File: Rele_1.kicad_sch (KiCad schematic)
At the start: 5 parts

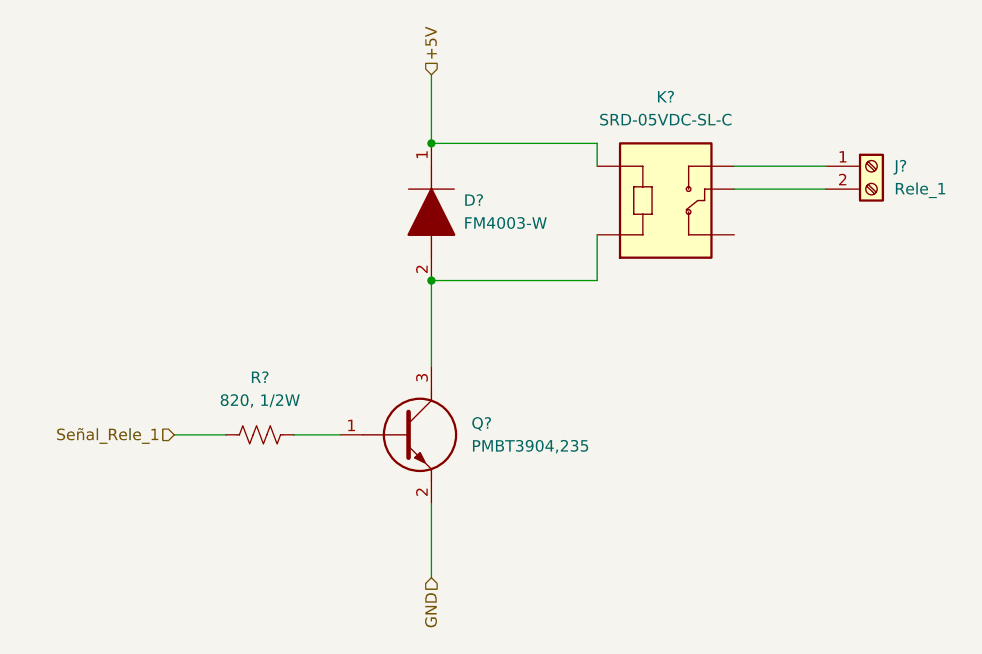
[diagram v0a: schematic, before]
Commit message: Ajuste del esquematico
Se cambio el integrado ESP32 por 2 tiras de pines de 1x15, se quitaron los switches EN y BOOT que ya estan en el NodeMCU, se quito el mutliplexor 74HC y se cablearon las I/O
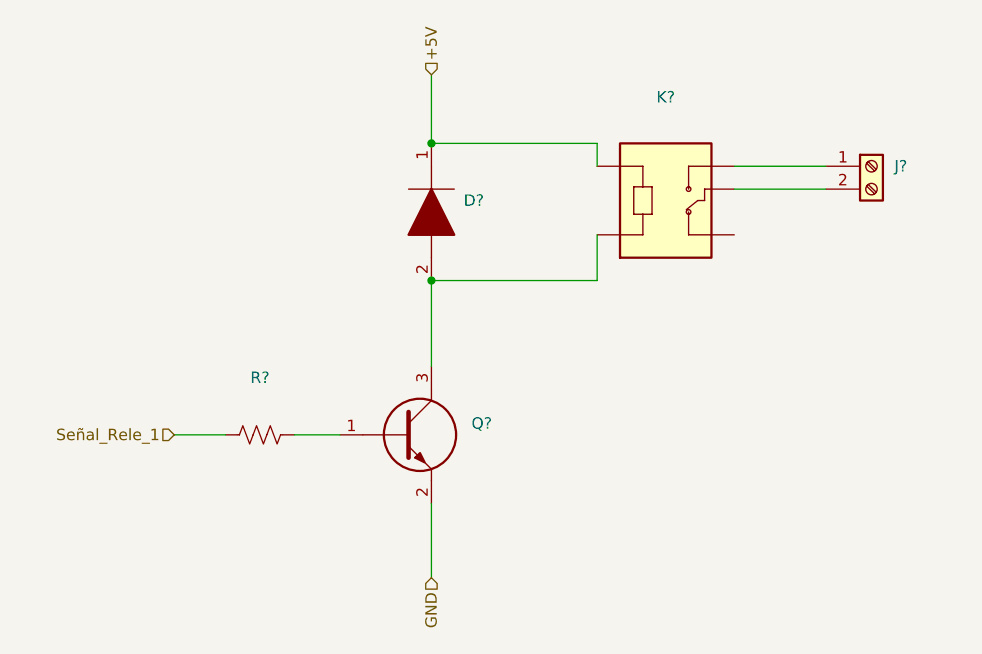
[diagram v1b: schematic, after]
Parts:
- D?: value FM4003-W -> (none); footprint DIOM5025X231N -> (none)
- J?: value Rele_1 -> (none)
- K?: value SRD-05VDC-SL-C -> (none); footprint RELAY_SRD-05VDC-SL-C -> (none)
- Q?: value PMBT3904,235 -> (none); footprint SOT95P230X110-3N -> (none)
- R?: value 820, 1/2W -> (none)
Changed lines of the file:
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@@
       (effects (font (size 1.27 1.27)) (justify left))
     )
-    (property "Value" "FM4003-W" (id 1) (at 143.2814 78.7399 90)
+    (property "Value" "" (id 1) (at 143.2814 78.7399 90)
       (effects (font (size 1.27 1.27)) (justify left))
     )
-    (property "Footprint" "DIOM5025X231N" (id 2) (at 139.7 81.28 0)
+    (property "Footprint" "" (id 2) (at 139.7 81.28 0)
       (effects (font (size 1.27 1.27)) (justify left) hide)
     )
@@
     (in_bom yes) (on_board yes) (fields_autoplaced)
     (property "Reference" "K?" (id 0) (at 165.735 64.7192 0))
-    (property "Value" "SRD-05VDC-SL-C" (id 1) (at 165.735 67.2592 0))
-    (property "Footprint" "RELAY_SRD-05VDC-SL-C" (id 2) (at 165.735 74.93 0)
+    (property "Value" "" (id 1) (at 165.735 67.2592 0))
+    (property "Footprint" "" (id 2) (at 165.735 74.93 0)
       (effects (font (size 1.27 1.27)) (justify left bottom) hide)
     )
@@
       (effects (font (size 1.27 1.27)) (justify left))
     )
-    (property "Value" "Rele_1" (id 1) (at 191.135 74.9299 0)
+    (property "Value" "" (id 1) (at 191.135 74.9299 0)
       (effects (font (size 1.27 1.27)) (justify left))
     )
@@
       (effects (font (size 1.27 1.27)) (justify left))
     )
-    (property "Value" "PMBT3904,235" (id 1) (at 144.145 103.5049 0)
+    (property "Value" "" (id 1) (at 144.145 103.5049 0)
       (effects (font (size 1.27 1.27)) (justify left))
     )
-    (property "Footprint" "SOT95P230X110-3N" (id 2) (at 143.51 106.045 0)
+    (property "Footprint" "" (id 2) (at 143.51 106.045 0)
       (effects (font (size 1.27 1.27)) (justify left) hide)
     )
@@
     (in_bom yes) (on_board yes) (fields_autoplaced)
     (property "Reference" "R?" (id 0) (at 120.65 95.885 90))
-    (property "Value" "820, 1/2W" (id 1) (at 120.65 98.425 90))
+    (property "Value" "" (id 1) (at 120.65 98.425 90))
     (property "Footprint" "" (id 2) (at 120.904 101.219 90)
       (effects (font (size 1.27 1.27)) hide)

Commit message: Modificación de posición de circ. filtrado y circ. de adaptación de tensión
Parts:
- D?, J?, K?, Q?, R?: value (none) -> ~
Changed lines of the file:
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@@
       (effects (font (size 1.27 1.27)) (justify left))
     )
-    (property "Value" "" (id 1) (at 143.2814 78.7399 90)
+    (property "Value" "~" (id 1) (at 143.2814 78.7399 90)
       (effects (font (size 1.27 1.27)) (justify left))
     )
@@
     (in_bom yes) (on_board yes) (fields_autoplaced)
     (property "Reference" "K?" (id 0) (at 165.735 64.7192 0))
-    (property "Value" "" (id 1) (at 165.735 67.2592 0))
+    (property "Value" "~" (id 1) (at 165.735 67.2592 0))
     (property "Footprint" "" (id 2) (at 165.735 74.93 0)
       (effects (font (size 1.27 1.27)) (justify left bottom) hide)
@@
       (effects (font (size 1.27 1.27)) (justify left))
     )
-    (property "Value" "" (id 1) (at 191.135 74.9299 0)
+    (property "Value" "~" (id 1) (at 191.135 74.9299 0)
       (effects (font (size 1.27 1.27)) (justify left))
     )
@@
       (effects (font (size 1.27 1.27)) (justify left))
     )
-    (property "Value" "" (id 1) (at 144.145 103.5049 0)
+    (property "Value" "~" (id 1) (at 144.145 103.5049 0)
       (effects (font (size 1.27 1.27)) (justify left))
     )
@@
     (in_bom yes) (on_board yes) (fields_autoplaced)
     (property "Reference" "R?" (id 0) (at 120.65 95.885 90))
-    (property "Value" "" (id 1) (at 120.65 98.425 90))
+    (property "Value" "~" (id 1) (at 120.65 98.425 90))
     (property "Footprint" "" (id 2) (at 120.904 101.219 90)
       (effects (font (size 1.27 1.27)) hide)

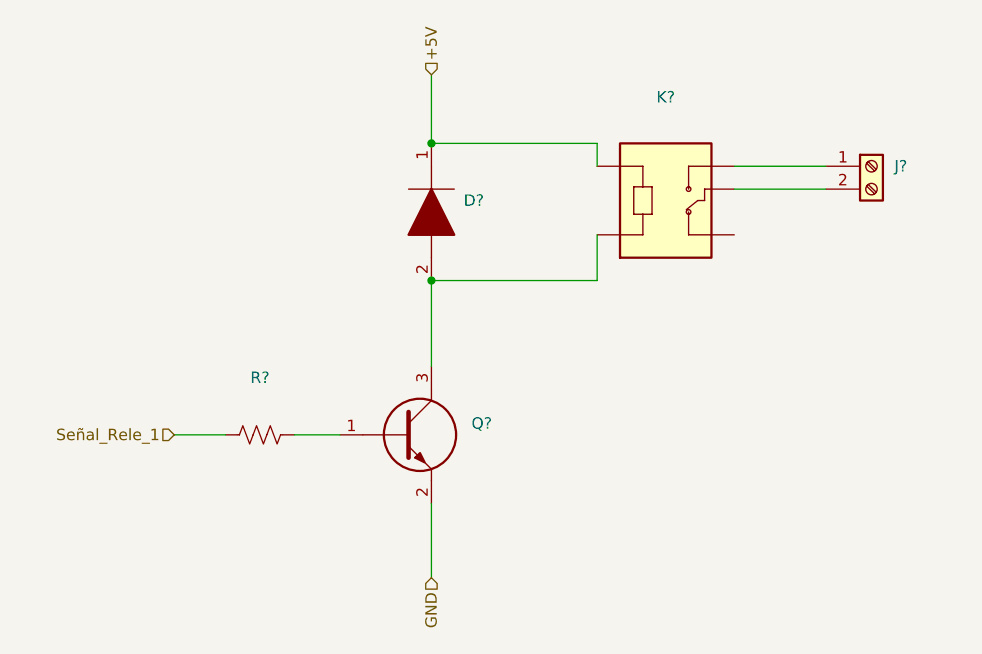
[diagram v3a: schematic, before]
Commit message: Actualización de SCH según placa industrial, y búsqueda de footprints.
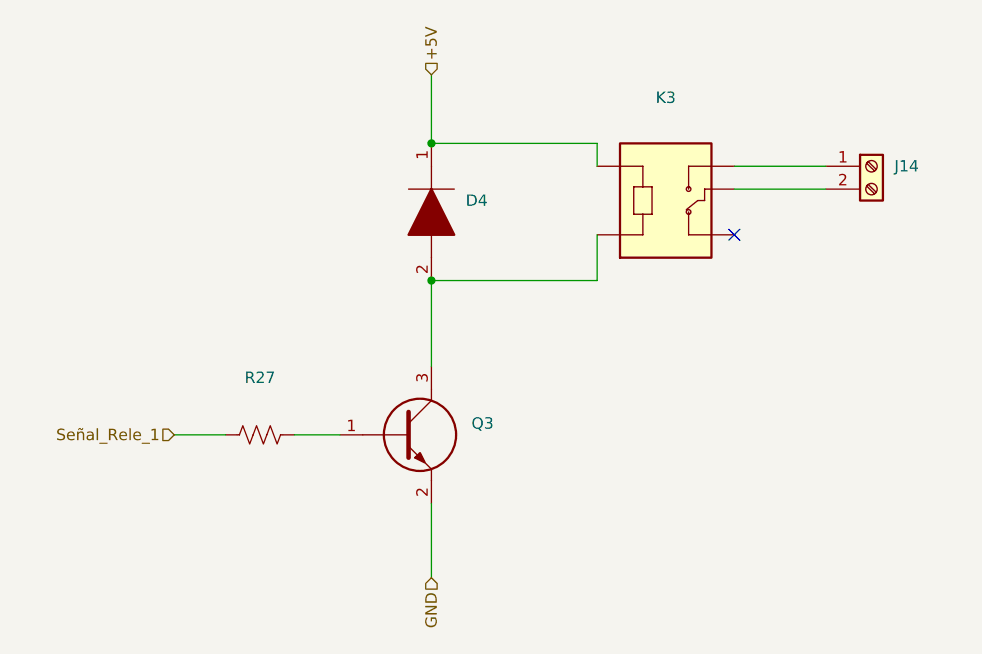
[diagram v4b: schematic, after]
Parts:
- D4: renamed from D?; value ~ -> (none)
- J14: renamed from J?; value ~ -> (none)
- K3: renamed from K?; value ~ -> (none)
- Q3: renamed from Q?; value ~ -> (none)
- R27: renamed from R?; value ~ -> (none)
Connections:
- no-connect marks 0 -> 1
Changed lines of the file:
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@@
   (junction (at 139.7 69.85) (diameter 0) (color 0 0 0 0)
   )
+  (no_connect (at 173.355 80.01))
   (wire (pts (xy 139.7 85.09) (xy 139.7 94.615))
     (stroke (width 0) (type default) (color 0 0 0 0))
@@
   (symbol (lib_id "FM4003-W:FM4003-W") (at 139.7 69.85 270) (unit 1)
     (in_bom yes) (on_board yes) (fields_autoplaced)
-    (property "Reference" "D?" (id 0) (at 143.2814 76.1999 90)
+    (property "Reference" "D4" (id 0) (at 143.51 76.1999 90)
       (effects (font (size 1.27 1.27)) (justify left))
     )
-    (property "Value" "~" (id 1) (at 143.2814 78.7399 90)
+    (property "Value" "" (id 1) (at 143.51 78.7399 90)
       (effects (font (size 1.27 1.27)) (justify left))
     )
@@
   (symbol (lib_id "SRD-05VDC-SL-C:SRD-05VDC-SL-C") (at 165.735 74.93 0) (unit 1)
     (in_bom yes) (on_board yes) (fields_autoplaced)
-    (property "Reference" "K?" (id 0) (at 165.735 64.7192 0))
-    (property "Value" "~" (id 1) (at 165.735 67.2592 0))
+    (property "Reference" "K3" (id 0) (at 165.735 64.77 0))
+    (property "Value" "" (id 1) (at 165.735 67.31 0))
     (property "Footprint" "" (id 2) (at 165.735 74.93 0)
       (effects (font (size 1.27 1.27)) (justify left bottom) hide)
@@
   (symbol (lib_id "Connector:Screw_Terminal_01x02") (at 188.595 72.39 0) (unit 1)
     (in_bom yes) (on_board yes) (fields_autoplaced)
-    (property "Reference" "J?" (id 0) (at 191.135 72.3899 0)
+    (property "Reference" "J14" (id 0) (at 191.135 72.3899 0)
       (effects (font (size 1.27 1.27)) (justify left))
     )
-    (property "Value" "~" (id 1) (at 191.135 74.9299 0)
+    (property "Value" "" (id 1) (at 191.135 74.9299 0)
       (effects (font (size 1.27 1.27)) (justify left))
     )
@@
   (symbol (lib_id "PMBT3904,235:PMBT3904,235") (at 129.54 102.235 0) (unit 1)
     (in_bom yes) (on_board yes) (fields_autoplaced)
-    (property "Reference" "Q?" (id 0) (at 144.145 100.9649 0)
+    (property "Reference" "Q3" (id 0) (at 144.145 100.9649 0)
       (effects (font (size 1.27 1.27)) (justify left))
     )
-    (property "Value" "~" (id 1) (at 144.145 103.5049 0)
+    (property "Value" "" (id 1) (at 144.145 103.5049 0)
       (effects (font (size 1.27 1.27)) (justify left))
     )
@@
   (symbol (lib_id "Device:R_US") (at 120.65 102.235 90) (unit 1)
     (in_bom yes) (on_board yes) (fields_autoplaced)
-    (property "Reference" "R?" (id 0) (at 120.65 95.885 90))
-    (property "Value" "~" (id 1) (at 120.65 98.425 90))
+    (property "Reference" "R27" (id 0) (at 120.65 95.885 90))
+    (property "Value" "" (id 1) (at 120.65 98.425 90))
     (property "Footprint" "" (id 2) (at 120.904 101.219 90)
       (effects (font (size 1.27 1.27)) hide)

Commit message: Fin de SCH, config de inicio para PCB
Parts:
- D4: value (none) -> FM4003-W; footprint (none) -> FM4003W:DIOM5025X231N
- J14: value (none) -> Rele_1; footprint (none) -> TB002-500-02BE:TB00250002BE
- K3: value (none) -> SRD-05VDC-SL-C; footprint (none) -> SRD-05VDC-SL-C-Version_2:RELAY_SRD-05VDC-SL-C
- Q3: value (none) -> PMBT3904,235; footprint (none) -> PMBT3904,235:SOT95P230X110-3N
- R27: value (none) -> 820, 1/2W; footprint (none) -> Resistor_SMD:R_0805_2012Metric
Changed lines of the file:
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@@
       (effects (font (size 1.27 1.27)) (justify left))
     )
-    (property "Value" "" (id 1) (at 143.51 78.7399 90)
+    (property "Value" "FM4003-W" (id 1) (at 143.51 78.7399 90)
       (effects (font (size 1.27 1.27)) (justify left))
     )
-    (property "Footprint" "" (id 2) (at 139.7 81.28 0)
+    (property "Footprint" "FM4003W:DIOM5025X231N" (id 2) (at 139.7 81.28 0)
       (effects (font (size 1.27 1.27)) (justify left) hide)
     )
@@
     (in_bom yes) (on_board yes) (fields_autoplaced)
     (property "Reference" "K3" (id 0) (at 165.735 64.77 0))
-    (property "Value" "" (id 1) (at 165.735 67.31 0))
-    (property "Footprint" "" (id 2) (at 165.735 74.93 0)
+    (property "Value" "SRD-05VDC-SL-C" (id 1) (at 165.735 67.31 0))
+    (property "Footprint" "SRD-05VDC-SL-C-Version_2:RELAY_SRD-05VDC-SL-C" (id 2) (at 165.735 74.93 0)
       (effects (font (size 1.27 1.27)) (justify left bottom) hide)
     )
@@
       (effects (font (size 1.27 1.27)) (justify left))
     )
-    (property "Value" "" (id 1) (at 191.135 74.9299 0)
+    (property "Value" "Rele_1" (id 1) (at 191.135 74.9299 0)
       (effects (font (size 1.27 1.27)) (justify left))
     )
-    (property "Footprint" "" (id 2) (at 188.595 72.39 0)
+    (property "Footprint" "TB002-500-02BE:TB00250002BE" (id 2) (at 188.595 72.39 0)
       (effects (font (size 1.27 1.27)) hide)
     )
@@
       (effects (font (size 1.27 1.27)) (justify left))
     )
-    (property "Value" "" (id 1) (at 144.145 103.5049 0)
+    (property "Value" "PMBT3904,235" (id 1) (at 144.145 103.5049 0)
       (effects (font (size 1.27 1.27)) (justify left))
     )
-    (property "Footprint" "" (id 2) (at 143.51 106.045 0)
+    (property "Footprint" "PMBT3904,235:SOT95P230X110-3N" (id 2) (at 143.51 106.045 0)
       (effects (font (size 1.27 1.27)) (justify left) hide)
     )
@@
     (in_bom yes) (on_board yes) (fields_autoplaced)
     (property "Reference" "R27" (id 0) (at 120.65 95.885 90))
-    (property "Value" "" (id 1) (at 120.65 98.425 90))
-    (property "Footprint" "" (id 2) (at 120.904 101.219 90)
+    (property "Value" "820, 1/2W" (id 1) (at 120.65 98.425 90))
+    (property "Footprint" "Resistor_SMD:R_0805_2012Metric" (id 2) (at 120.904 101.219 90)
       (effects (font (size 1.27 1.27)) hide)
     )

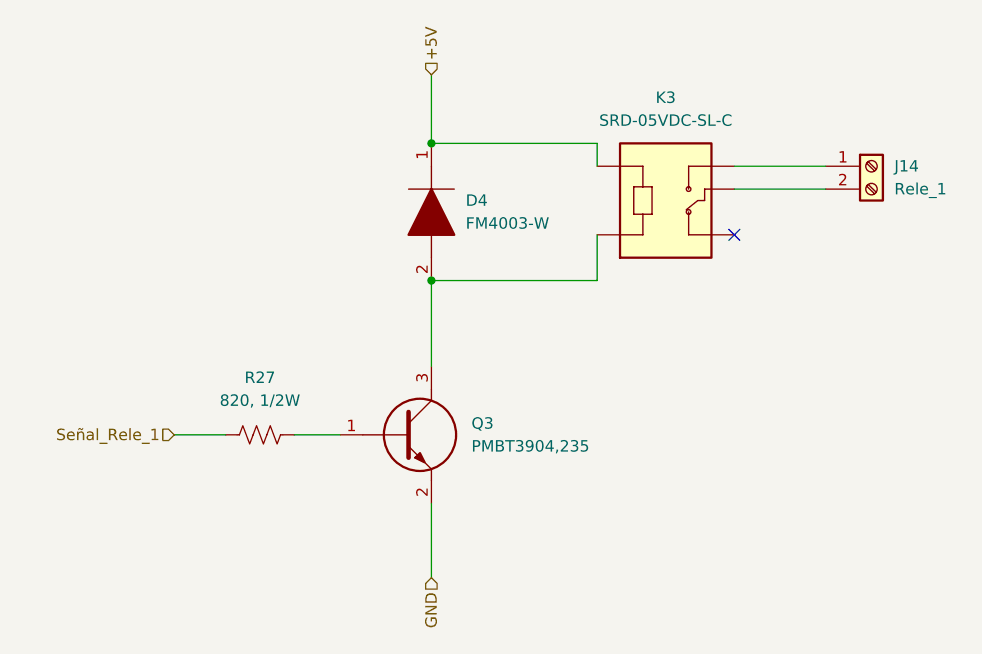
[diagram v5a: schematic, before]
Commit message: Cambios en SCH y PCB.
Se cambio el adaptador de nivel 5-3,3V por un circuito con MOSFET 2N7002, dado que ya no hay stock del NXB. Se modificó el footprint del expansor I/O por uno thorugh-hole.
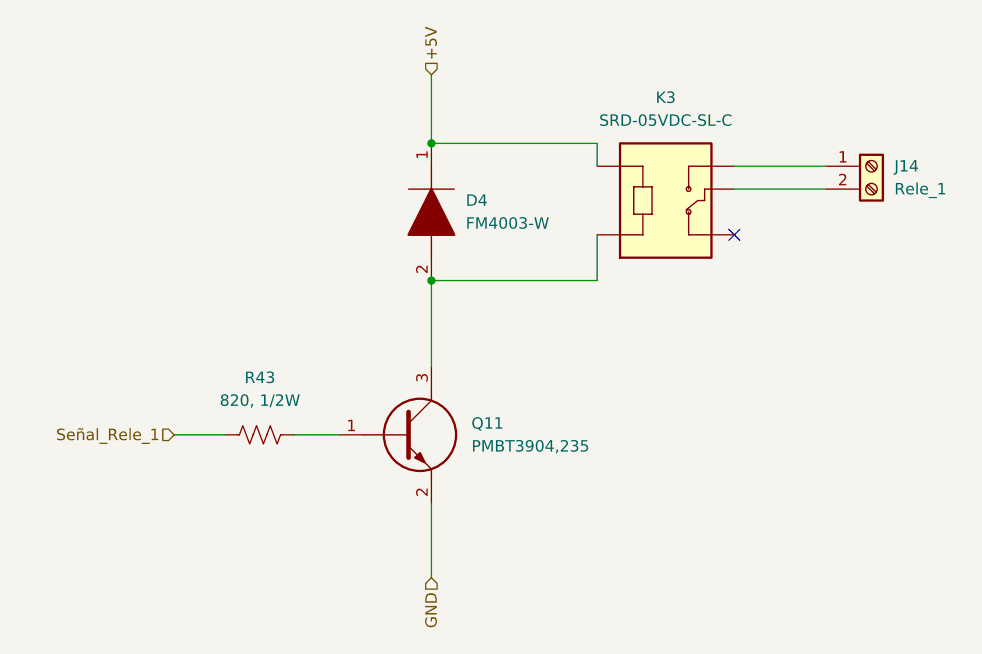
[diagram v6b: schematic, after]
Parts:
- renumbered Q3 to Q11, R27 to R43
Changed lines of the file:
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@@
   (symbol (lib_id "PMBT3904,235:PMBT3904,235") (at 129.54 102.235 0) (unit 1)
     (in_bom yes) (on_board yes) (fields_autoplaced)
-    (property "Reference" "Q3" (id 0) (at 144.145 100.9649 0)
+    (property "Reference" "Q11" (id 0) (at 144.145 100.9649 0)
       (effects (font (size 1.27 1.27)) (justify left))
     )
@@
   (symbol (lib_id "Device:R_US") (at 120.65 102.235 90) (unit 1)
     (in_bom yes) (on_board yes) (fields_autoplaced)
-    (property "Reference" "R27" (id 0) (at 120.65 95.885 90))
+    (property "Reference" "R43" (id 0) (at 120.65 95.885 90))
     (property "Value" "820, 1/2W" (id 1) (at 120.65 98.425 90))
     (property "Footprint" "Resistor_SMD:R_0805_2012Metric" (id 2) (at 120.904 101.219 90)

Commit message: Se finalizó con el PCB del prototipo.
Dado que se buscó a toda costa que el PCB fuera de 1 capa, en varios puntos del circuito se tuvieron que agregar pin headers individuales para conectar a 3V3 y GND, junto con tiras de pin headers. Cada una de estas se conectara luego entre si mediante cables.

Tambien se generaron los archivos Gerber y BOM.
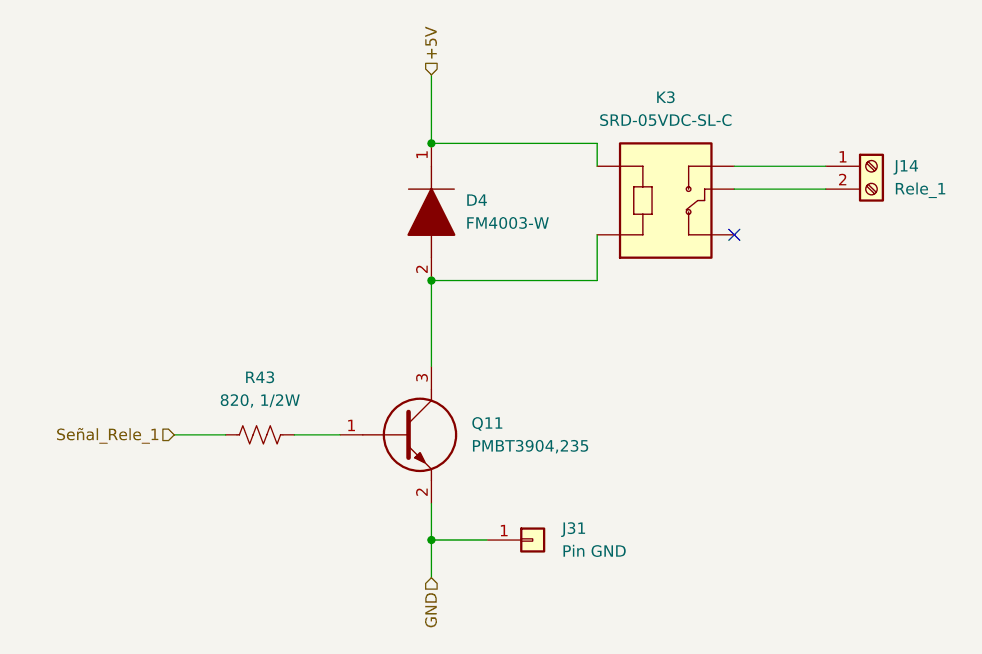
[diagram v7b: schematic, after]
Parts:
- added J31: Pin GND, Connector_PinHeader_2.54mm:PinHeader_1x01_P2.54mm_Vertical, symbol Connector_Generic:Conn_01x01
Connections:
- net GND: now also J31.1 (Pin_1)
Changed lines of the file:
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@@
   (junction (at 139.7 85.09) (diameter 0) (color 0 0 0 0)
+  )
+  (junction (at 139.7 113.919) (diameter 0) (color 0 0 0 0)
   )
   (junction (at 139.7 69.85) (diameter 0) (color 0 0 0 0)
@@
   )
   (wire (pts (xy 139.7 69.85) (xy 158.115 69.85))
+    (stroke (width 0) (type default) (color 0 0 0 0))
+  )
+  (wire (pts (xy 139.7 113.919) (xy 139.7 118.11))
+    (stroke (width 0) (type default) (color 0 0 0 0))
+  )
+  (wire (pts (xy 139.7 113.919) (xy 145.8722 113.919))
     (stroke (width 0) (type default) (color 0 0 0 0))
   )
@@
     (stroke (width 0) (type default) (color 0 0 0 0))
   )
-  (wire (pts (xy 139.7 109.855) (xy 139.7 118.11))
+  (wire (pts (xy 139.7 109.855) (xy 139.7 113.919))
     (stroke (width 0) (type default) (color 0 0 0 0))
   )
@@
     (pin "2")
   )
+  (symbol (lib_id "Connector_Generic:Conn_01x01") (at 150.9522 113.919 0) (unit 1)
+    (in_bom yes) (on_board yes) (fields_autoplaced)
+    (property "Reference" "J31" (id 0) (at 154.2034 112.6489 0)
+      (effects (font (size 1.27 1.27)) (justify left))
+    )
+    (property "Value" "Pin GND" (id 1) (at 154.2034 115.1889 0)
+      (effects (font (size 1.27 1.27)) (justify left))
+    )
+    (property "Footprint" "Connector_PinHeader_2.54mm:PinHeader_1x01_P2.54mm_Vertical" (id 2) (at 150.9522 113.919 0)
+      (effects (font (size 1.27 1.27)) hide)
+    )
+    (property "Datasheet" "~" (id 3) (at 150.9522 113.919 0)
+      (effects (font (size 1.27 1.27)) hide)
+    )
+    (pin "1")
+  )
   (symbol (lib_id "SRD-05VDC-SL-C:SRD-05VDC-SL-C") (at 165.735 74.93 0) (unit 1)
